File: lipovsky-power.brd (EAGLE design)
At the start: 50 x 32 mm, 93 parts, among them J1 M04-929J, J2 M04-929J, J3 M04-929J, J4 M04-929J, Q1 NMOS30V_30A, Q12 NMOS40V_10A, Q14 NMOS40V_10A, Q16 NMOS40V_10A, Q18 NMOS40V_10A, Q21 PMOS30V_11A, Q22 PMOS30V_11A, Q23 NMOS40V_10A, Q24 NMOS40V_10A, Q25 PMOS30V_11A, Q26 PMOS30V_11A, Q27 NMOS40V_10A, Q28 NMOS40V_10A, Q3 2PMOS50V_0.17A, Q31 PMOS30V_11A, Q32 PMOS30V_11A, Q33 PMOS30V_11A, Q34 PMOS30V_11A, Q35 PMOS30V_11A, Q36 PMOS30V_11A, Q37 PMOS30V_11A, Q38 PMOS30V_11A, Q4 2PMOS50V_0.17A, Q41 PMOS30V_11A, Q42 PMOS30V_11A, Q43 PMOS30V_11A, Q44 PMOS30V_11A, Q45 PMOS30V_11A, Q46 PMOS30V_11A, Q47 PMOS30V_11A, Q48 PMOS30V_11A, Q51 PMOS30V_11A, Q52 PMOS30V_11A, Q53 PMOS30V_11A, Q54 PMOS30V_11A, Q55 PMOS30V_11A, Q56 PMOS30V_11A, Q57 PMOS30V_11A, Q58 PMOS30V_11A, Q62 PMOS30V_11A, Q64 PMOS30V_11A, Q66 PMOS30V_11A, Q68 PMOS30V_11A, U1 LTC3805-5IDD, U2 ATTINYX4A2MMHR, U3 DG508BEN-T1-GE4, U4 DG508BEN-T1-GE4, U5 LM2665M6

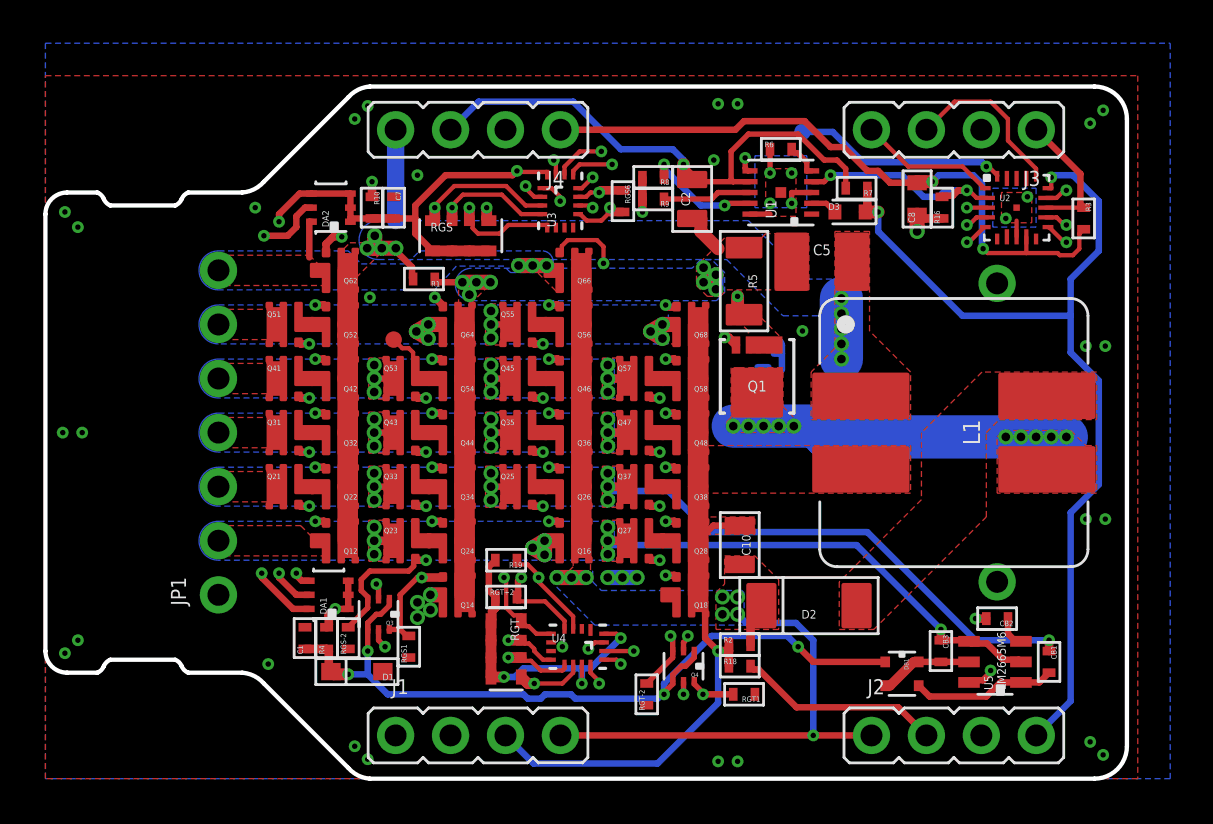
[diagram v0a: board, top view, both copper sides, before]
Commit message: Control board compacted
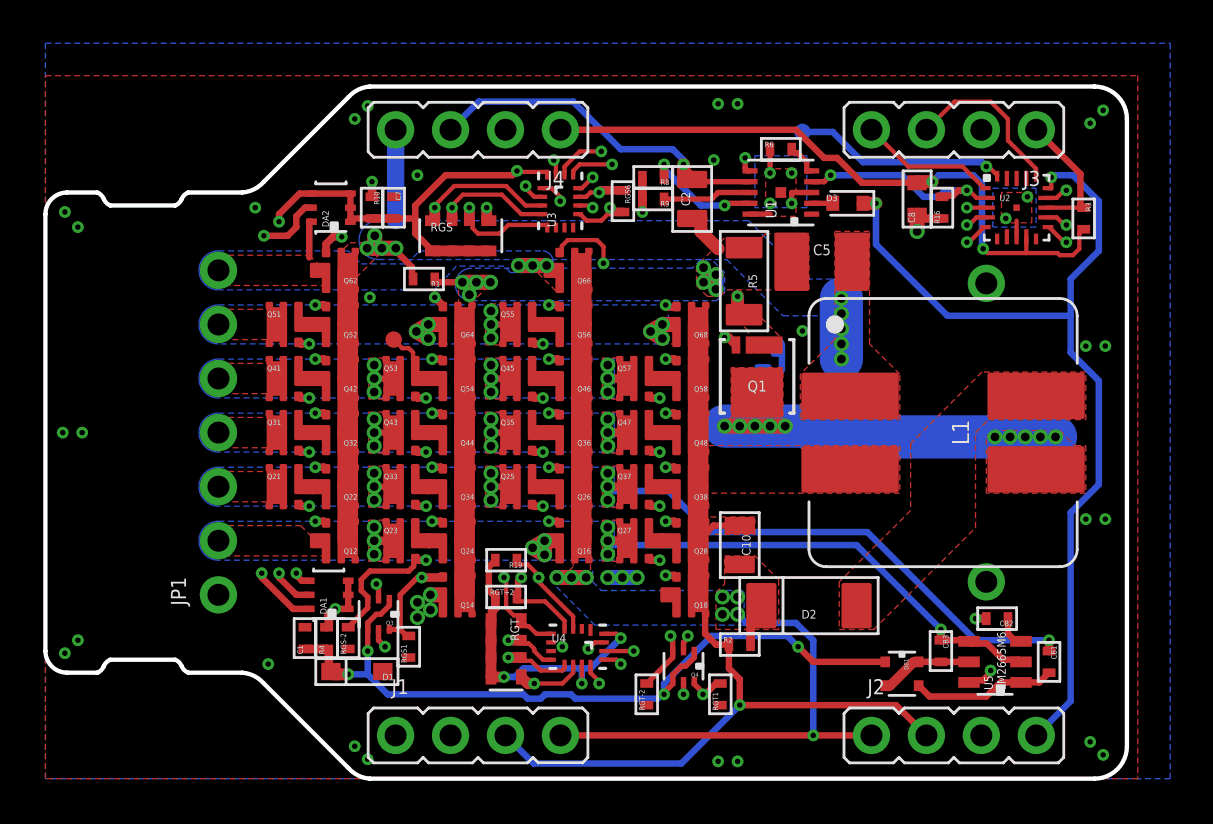
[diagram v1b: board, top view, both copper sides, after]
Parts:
- removed R18: RES1K_16, dubec:0402
- removed R7: RES18.2K_16, dubec:0402
- moved RGT1 1.10 mm to (31.2, 3.90), turned to 90 degrees
- moved L1 0.50 mm to (41.5, 16.0)
- moved D3 0.41 mm to (37.1, 26.6)
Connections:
- removed net FB: D3.C, J2.4, R7.1, U2.15
- removed net OPTO_C: J2.2, R18.2
- new net TH: D3.C, J2.4, U2.15
- net +8V: no longer R7.2
- net T-: now also J2.2; no longer R18.1
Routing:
- net FB: track 43.5 -> 0.00 mm, vias 2 -> 0
- net TH: track 0.00 -> 43.2 mm, vias 0 -> 2
- net T-: track 33.5 -> 43.0 mm
- net OPTO_C: track 9.46 -> 0.00 mm
- net +8V: track 24.8 -> 16.2 mm
- net N$10: track 26.8 -> 29.5 mm

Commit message: tidy
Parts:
- removed C10: CAP47UF_10V, dubec:0805
- added CTARGET: CAP100UF_10V, dubec:1210
- renumbered C5 to CSOURCE, D2 to DT1, R5 to RSSENSE
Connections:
- net T+: now also CTARGET.2; no longer C10.2
- net T-: now also CTARGET.1; no longer C10.1
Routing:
- net T-: track 43.0 -> 40.7 mm
- net SDA: track 7.83 -> 6.17 mm
- net S-: track 26.7 -> 25.8 mm, vias 28 -> 30
- net TH: track 43.2 -> 42.6 mm
- net BATT-: vias 28 -> 30

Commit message: Removed 2S booster
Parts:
- removed CB1, CB2, CB3: CAP4.7UF_10V, dubec:0402
- removed DB1: 2D_SCHOTTKY40V_0.2A, dubec:SOT-563
- removed U5: LM2665M6, dubec:SOT-23-6
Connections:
- removed net 2SBOOST: CB3.2, DB1.2, DB1.4, U5.5
- removed net N$11: CB2.1, U5.3
- removed net N$2: CB1.2, DB1.3, U5.1
- removed net N$9: CB2.2, U5.6
- net C1: no longer CB3.1, U5.2, U5.4
- net C2: no longer CB1.1
- net C4+: no longer DB1.1
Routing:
- net C2: track 42.5 -> 18.6 mm, vias 11 -> 9
- net C1: track 34.3 -> 12.6 mm, vias 10 -> 8
- net C4+: track 37.3 -> 25.1 mm, vias 4 -> 3
- net N$2: track 6.69 -> 0.00 mm
- net N$9: track 4.48 -> 0.00 mm, vias 2 -> 0
- net 2SBOOST: track 4.33 -> 0.00 mm
- net T+: track 46.4 -> 43.9 mm
- net N$11: track 1.44 -> 0.00 mm

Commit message: S-F
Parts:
- moved C2 0.20 mm to (30.1, 26.8)
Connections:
- new net S-F: C2.1, C8.1, J2.3, J3.2, R16.1, R6.1, U1.10, U1.3, U1.PAD, U2.8, U2.PAD, U3.12, U4.12
- net S-: no longer C2.1, C8.1, J2.3, J3.2, R16.1, R6.1, U1.10, U1.3, U1.PAD, U2.8, U2.PAD, U3.12, U4.12
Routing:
- net S-F: track 0.00 -> 98.0 mm, vias 0 -> 10
- net S-: track 25.8 -> 15.1 mm, vias 30 -> 21
- added copper zone on layer 1, net S-F
- added copper zone on layer 16, net S-F

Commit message: routing
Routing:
- net S-F: track 98.0 -> 97.5 mm
- net AT0: track 39.7 -> 39.2 mm
- net AT2: track 36.0 -> 35.5 mm
- net AT1: track 36.3 -> 35.8 mm
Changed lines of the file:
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@@
 <wire x1="23.81" y1="2" x2="23.91" y2="1.9" width="0.3" layer="15"/>
 <wire x1="23.91" y1="1.9" x2="32.8" y2="1.9" width="0.3" layer="15"/>
-<wire x1="32.6" y1="7.1" x2="33.1" y2="8" width="0" layer="19" extent="1-1"/>
-<wire x1="32.8" y1="6.6" x2="32.6" y2="6.2" width="0" layer="19" extent="1-16"/>
-<wire x1="33" y1="11.2" x2="32" y2="8.4" width="0" layer="19" extent="1-15"/>
-<wire x1="25" y1="9.3" x2="31.3" y2="8.4" width="0" layer="19" extent="1-1"/>
-<wire x1="24.325" y1="9.3" x2="23.65" y2="9.3" width="0" layer="19" extent="1-1"/>
-<wire x1="24.775" y1="11" x2="25" y2="9.3" width="0" layer="19" extent="1-1"/>
 </signal>
 <signal name="GT3">
@@
 <via x="23.5" y="28.6" extent="1-16" drill="0.25"/>
 <wire x1="23.5" y1="28.6" x2="24.4" y2="28.6" width="0.2" layer="15"/>
-<wire x1="24.4" y1="28.6" x2="26.3" y2="30.5" width="0.2" layer="15"/>
+<wire x1="24.4" y1="28.6" x2="25.4" y2="29.6" width="0.2" layer="15"/>
+<wire x1="25.4" y1="29.6" x2="26.4" y2="29.6" width="0.2" layer="15"/>
+<wire x1="26.4" y1="29.6" x2="27.3" y2="30.5" width="0.2" layer="15"/>
 <wire x1="23.6" y1="27.925" x2="23.6" y2="28.5" width="0.2" layer="1"/>
 <wire x1="23.6" y1="28.5" x2="23.5" y2="28.6" width="0.2" layer="1"/>
@@
 <wire x1="39.1" y1="28" x2="37.9" y2="28" width="0.2" layer="15"/>
 <wire x1="37.9" y1="28" x2="35.4" y2="30.5" width="0.2" layer="15"/>
-<wire x1="35.4" y1="30.5" x2="26.3" y2="30.5" width="0.2" layer="15"/>
+<wire x1="35.4" y1="30.5" x2="27.3" y2="30.5" width="0.2" layer="15"/>
 </signal>
 <signal name="AS1">
@@
 <wire x1="38.9" y1="27.6" x2="37.7" y2="27.6" width="0.2" layer="15"/>
 <wire x1="37.7" y1="27.6" x2="35.2" y2="30.1" width="0.2" layer="15"/>
-<wire x1="35.2" y1="30.1" x2="26.8" y2="30.1" width="0.2" layer="15"/>
-<wire x1="26.8" y1="30.1" x2="25.7" y2="29" width="0.2" layer="15"/>
+<wire x1="35.2" y1="30.1" x2="27.5" y2="30.1" width="0.2" layer="15"/>
+<wire x1="27.5" y1="30.1" x2="26.5" y2="29.1" width="0.2" layer="15"/>
+<wire x1="26.5" y1="29.1" x2="26.4" y2="29" width="0.2" layer="15"/>
+<wire x1="26.4" y1="29" x2="25.7" y2="29" width="0.2" layer="15"/>
 </signal>
 <signal name="AS2">
@@
 <wire x1="38.7" y1="27.2" x2="37.5" y2="27.2" width="0.2" layer="15"/>
 <wire x1="37.5" y1="27.2" x2="35" y2="29.7" width="0.2" layer="15"/>
-<wire x1="35" y1="29.7" x2="27.5" y2="29.7" width="0.2" layer="15"/>
-<wire x1="27.5" y1="29.7" x2="26.2" y2="28.4" width="0.2" layer="15"/>
+<wire x1="35" y1="29.7" x2="27.7" y2="29.7" width="0.2" layer="15"/>
+<wire x1="27.7" y1="29.7" x2="26.4" y2="28.4" width="0.2" layer="15"/>
+<wire x1="26.4" y1="28.4" x2="26.2" y2="28.4" width="0.2" layer="15"/>
 </signal>
 <signal name="AT0">
@@
 <wire x1="46.75" y1="26.85" x2="47.1" y2="27.2" width="0.2" layer="1"/>
 <wire x1="47.1" y1="27.2" x2="47.2" y2="27.2" width="0.2" layer="1"/>
-<wire x1="46.2" y1="26.2" x2="47.2" y2="27.2" width="0.2" layer="15"/>
+<wire x1="46.2" y1="25.5" x2="47.2" y2="26.5" width="0.2" layer="15"/>
+<wire x1="47.2" y1="26.5" x2="47.2" y2="27.2" width="0.2" layer="15"/>
 <wire x1="25.825" y1="6.3" x2="25.4" y2="6.3" width="0.2" layer="1"/>
 <wire x1="25.4" y1="6.3" x2="25.1" y2="6" width="0.2" layer="1"/>
-<wire x1="28.4" y1="5.6" x2="35.2" y2="5.6" width="0.2" layer="15"/>
-<wire x1="35.2" y1="5.6" x2="41.8" y2="12.2" width="0.2" layer="15"/>
-<wire x1="41.8" y1="12.2" x2="41.8" y2="17.3" width="0.2" layer="15"/>
+<wire x1="28.4" y1="5.6" x2="34.3" y2="5.6" width="0.2" layer="15"/>
+<wire x1="34.3" y1="5.6" x2="41.8" y2="13.1" width="0.2" layer="15"/>
+<wire x1="41.8" y1="13.1" x2="41.8" y2="17.3" width="0.2" layer="15"/>
 <wire x1="41.8" y1="17.3" x2="46.2" y2="21.7" width="0.2" layer="15"/>
-<wire x1="46.2" y1="21.7" x2="46.2" y2="26.2" width="0.2" layer="15"/>
+<wire x1="46.2" y1="21.7" x2="46.2" y2="25.5" width="0.2" layer="15"/>
 </signal>
 <signal name="AT1">
@@
 <wire x1="25.825" y1="5.9" x2="27.2" y2="5.9" width="0.2" layer="1"/>
 <wire x1="27.2" y1="5.9" x2="27.9" y2="5.2" width="0.2" layer="15"/>
-<wire x1="27.9" y1="5.2" x2="35.4" y2="5.2" width="0.2" layer="15"/>
+<wire x1="27.9" y1="5.2" x2="34.5" y2="5.2" width="0.2" layer="15"/>
 <contactref element="U2" pad="12"/>
 <via x="47.2" y="25.6" extent="1-16" drill="0.25"/>
@@
 <wire x1="46.6" y1="25.1" x2="47.1" y2="25.6" width="0.2" layer="15"/>
 <wire x1="47.1" y1="25.6" x2="47.2" y2="25.6" width="0.2" layer="15"/>
-<wire x1="35.4" y1="5.2" x2="42.2" y2="12" width="0.2" layer="15"/>
-<wire x1="42.2" y1="12" x2="42.2" y2="17.1" width="0.2" layer="15"/>
+<wire x1="34.5" y1="5.2" x2="42.2" y2="12.9" width="0.2" layer="15"/>
+<wire x1="42.2" y1="12.9" x2="42.2" y2="17.1" width="0.2" layer="15"/>
 <wire x1="42.2" y1="17.1" x2="46.6" y2="21.5" width="0.2" layer="15"/>
 <wire x1="46.6" y1="21.5" x2="46.6" y2="25.1" width="0.2" layer="15"/>
@@
 <wire x1="26.4" y1="5.5" x2="26.6" y2="5.3" width="0.2" layer="1"/>
 <wire x1="26.6" y1="5.3" x2="27.1" y2="4.8" width="0.2" layer="15"/>
-<wire x1="27.1" y1="4.8" x2="35.6" y2="4.8" width="0.2" layer="15"/>
+<wire x1="27.1" y1="4.8" x2="34.7" y2="4.8" width="0.2" layer="15"/>
 <contactref element="U2" pad="11"/>
 <via x="47.2" y="24.8" extent="1-16" drill="0.25"/>
@@
 <wire x1="46.4" y1="25.5" x2="47.1" y2="24.8" width="0.2" layer="1"/>
 <wire x1="47.1" y1="24.8" x2="47.2" y2="24.8" width="0.2" layer="1"/>
-<wire x1="35.6" y1="4.8" x2="42.6" y2="11.8" width="0.2" layer="15"/>
-<wire x1="42.6" y1="11.8" x2="42.6" y2="16.9" width="0.2" layer="15"/>
+<wire x1="34.7" y1="4.8" x2="42.6" y2="12.7" width="0.2" layer="15"/>
+<wire x1="42.6" y1="12.7" x2="42.6" y2="16.9" width="0.2" layer="15"/>
 <wire x1="42.6" y1="16.9" x2="47" y2="21.3" width="0.2" layer="15"/>
 <wire x1="47" y1="21.3" x2="47" y2="24.6" width="0.2" layer="15"/>
@@
 <wire x1="26.9" y1="3.1" x2="30.6" y2="3.1" width="0.3" layer="15"/>
 <wire x1="30.6" y1="3.1" x2="31.8" y2="4.3" width="0.3" layer="15"/>
-<wire x1="31.8" y1="4.3" x2="35.8" y2="4.3" width="0.3" layer="15"/>
-<wire x1="35.8" y1="4.3" x2="43.1" y2="11.6" width="0.3" layer="15"/>
-<wire x1="43.1" y1="11.6" x2="43.1" y2="16.7" width="0.3" layer="15"/>
+<wire x1="31.8" y1="4.3" x2="34.9" y2="4.3" width="0.3" layer="15"/>
+<wire x1="34.9" y1="4.3" x2="43.1" y2="12.5" width="0.3" layer="15"/>
+<wire x1="43.1" y1="12.5" x2="43.1" y2="16.7" width="0.3" layer="15"/>
 <wire x1="43.27" y1="2" x2="44.37" y2="3.1" width="0.3" layer="15"/>
 <wire x1="44.37" y1="3.1" x2="46.9" y2="3.1" width="0.3" layer="15"/>

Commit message: tidy
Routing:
- net S-F: track 97.5 -> 100.5 mm
- net TH: track 42.9 -> 42.3 mm

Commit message: TVS
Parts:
- added DTVS: D_ZENERSMBJ26D, dubec:DO-214AA+
- added R5, R7: RES100_16, dubec:0402
- moved C1 3.00 mm to (13.4, 3.85), turned to 0 degrees
- moved C7 1.00 mm to (16.1, 27.4)
- moved R10 1.00 mm to (15.1, 27.4)
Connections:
- new net C4D: DA1.1, DA1.2, DA1.3, R4.2, R7.1
- new net C6D: DA2.1, DA2.2, R5.1
- net BATT+: now also R5.2, R7.2; no longer DA1.1, DA1.2, DA1.3, DA2.1, DA2.2, R4.2
- net BATT-: now also DTVS.A
- net C6: now also DTVS.C
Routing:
- net C6: track 5.65 -> 10.1 mm, vias 3 -> 5
- net C4D: track 0.00 -> 3.77 mm
- net C6D: track 0.00 -> 1.95 mm
- net BATT-: track 17.9 -> 19.5 mm, vias 30 -> 32
- net BATT+: track 74.3 -> 73.8 mm

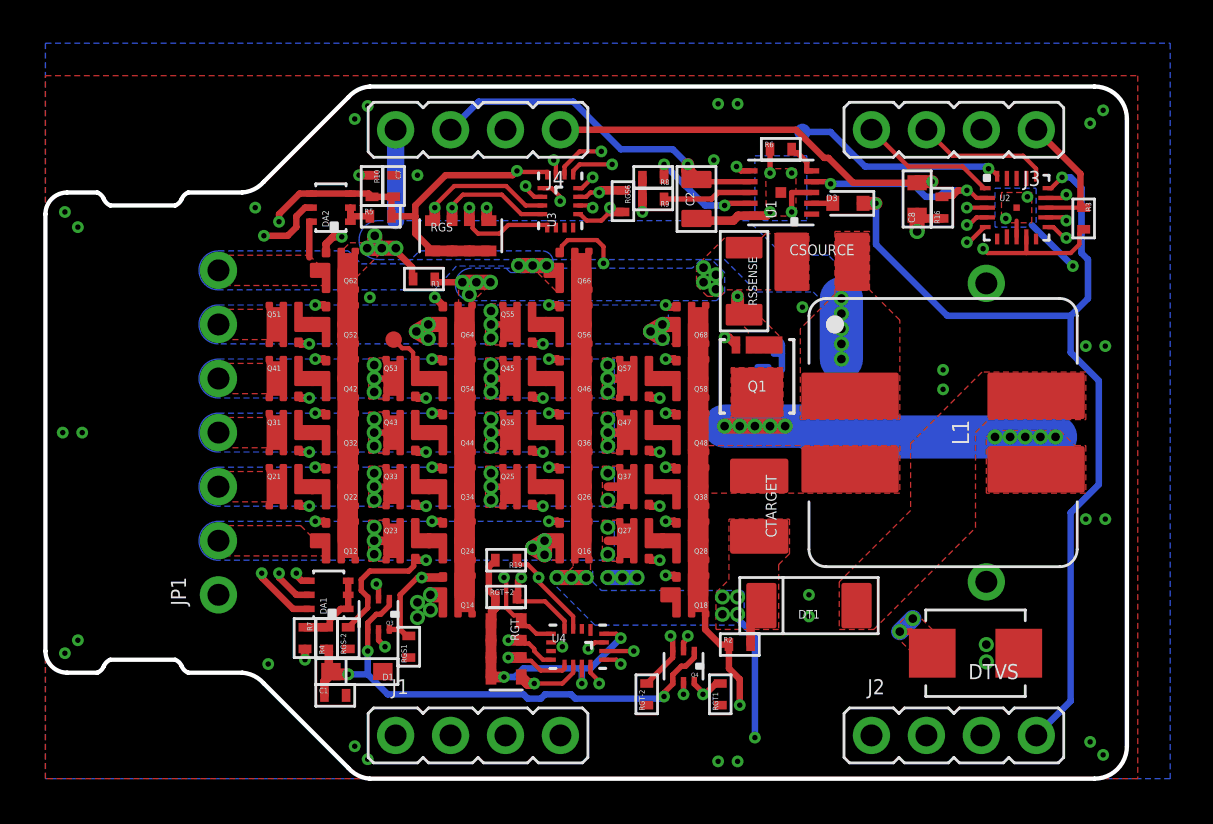
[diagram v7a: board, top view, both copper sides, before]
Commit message: prog testpoints
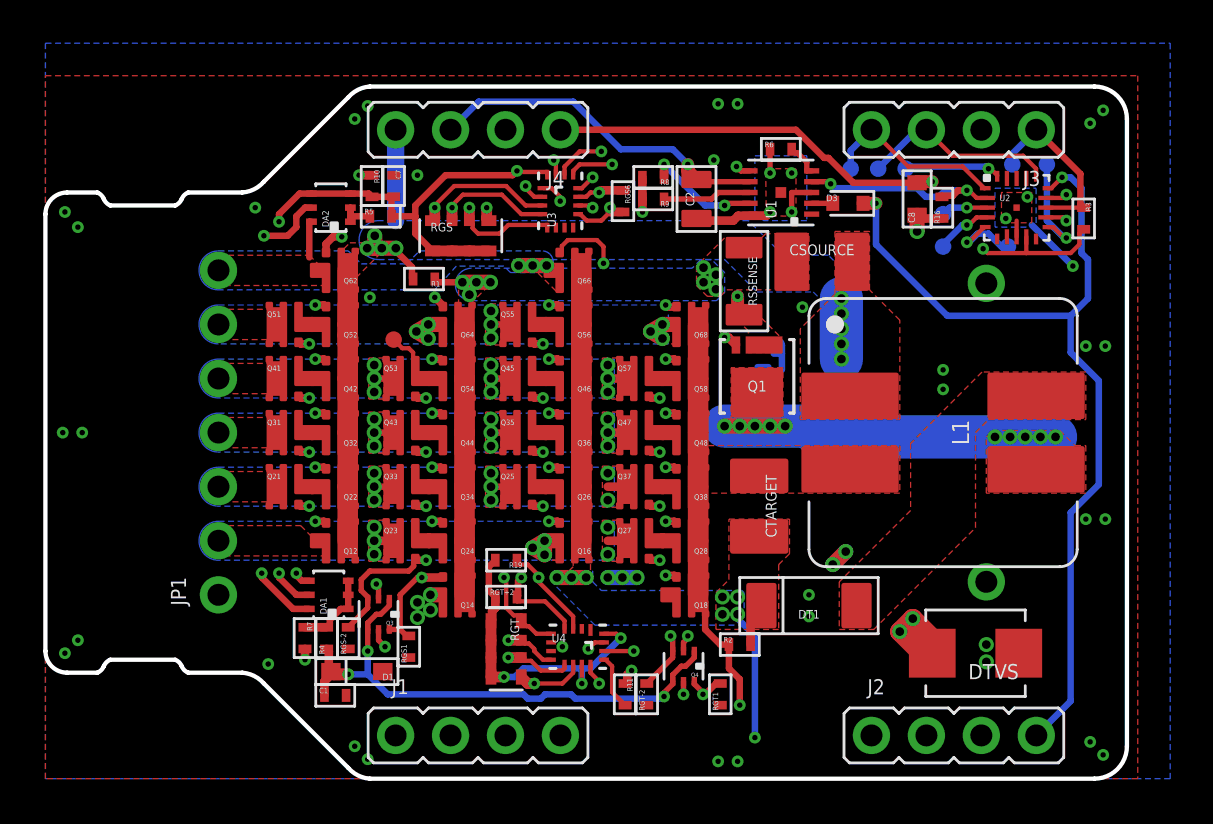
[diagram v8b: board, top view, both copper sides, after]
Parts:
- removed TP1: TEST-POINT3, SparkFun-Passives:PAD.03X.03
- added R11: RES1K_16, dubec:0402
- added TP_PA0, TP_PA1, TP_PA2, TP_PA4, TP_PA5, TP_PA6, TP_PB0, TP_PB3: TEST-POINT3, SparkFun-Passives:PAD.03X.03
- C1, C7: value CAP1UF_35V -> CAP2.2UF_35V
- R3: value RES5.1K_16 -> RES10K_16
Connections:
- new net SCI: R11.1, TP_PB0.P$1, U2.11
- net !S_RESET: now also TP_PB3.P$1
- net AS0: now also TP_PA2.P$1
- net AS1: now also TP_PA1.P$1
- net AS2: now also TP_PA0.P$1
- net AT2: now also R11.2; no longer U2.11
- net MISO: now also TP_PA5.P$1; no longer TP1.P$1
- net SCL: now also TP_PA4.P$1
- net SDA: now also TP_PA6.P$1
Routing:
- net SCI: track 0.00 -> 38.7 mm, vias 0 -> 2
- net C6: track 10.1 -> 48.3 mm, vias 5 -> 7
- net AT2: track 35.6 -> 2.55 mm, vias 2 -> 0
- net MISO: track 9.88 -> 4.49 mm
- net SDA: track 6.17 -> 9.14 mm
- net AS2: track 22.2 -> 24.5 mm
- net SCL: track 6.38 -> 8.58 mm
- net !S_RESET: track 6.26 -> 8.32 mm
- net AS1: track 22.7 -> 24.3 mm
- net AS0: track 23.3 -> 24.5 mm
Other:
- board text removed: "MISO"
